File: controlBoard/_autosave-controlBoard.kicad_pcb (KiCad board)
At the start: 2 copper layers, 37.5 x 35 mm, 33 parts, among them J2 Servo, SW1 SW_Push, SW2 SW_Push, U1 ATmega328P-AU, U2 PCA9685BS, U3 AP2112K-3.3TRG1, Y1 Crystal

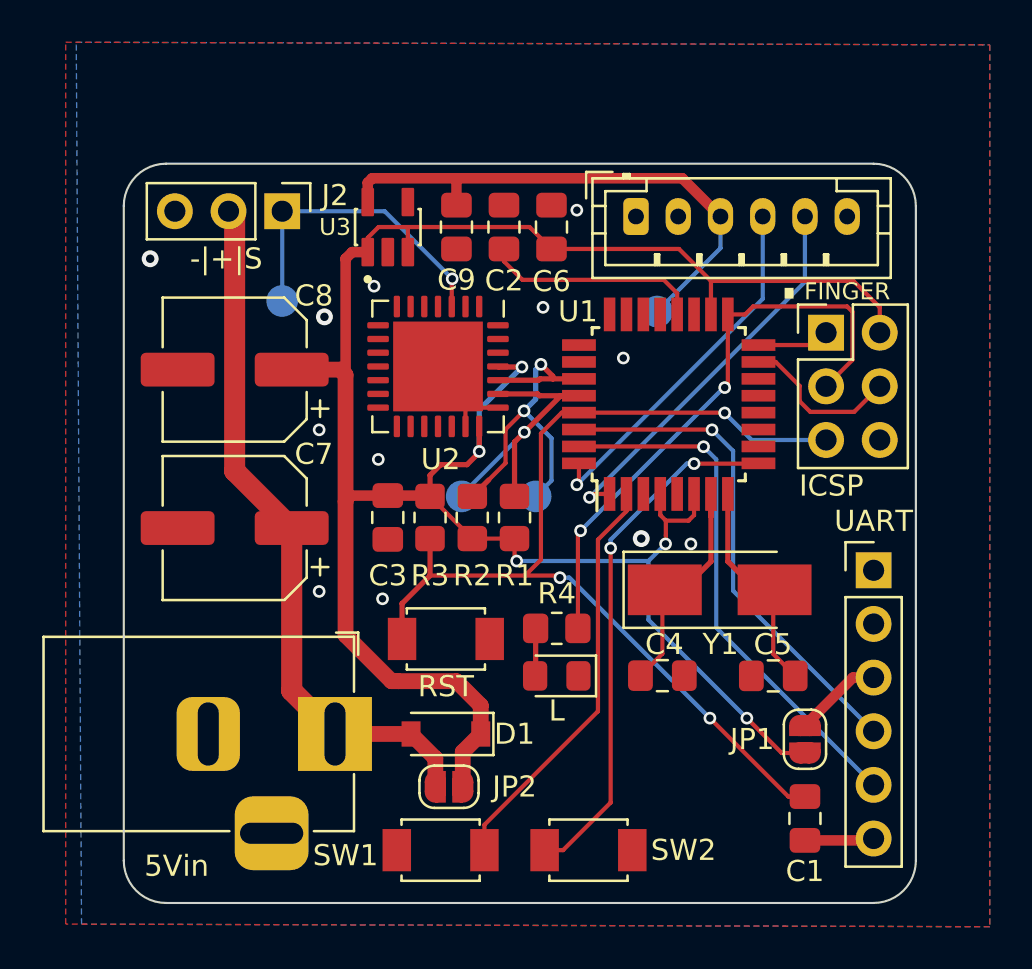
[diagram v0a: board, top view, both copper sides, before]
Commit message: Added decoupling cap for fingerprint reader, generated gerbers
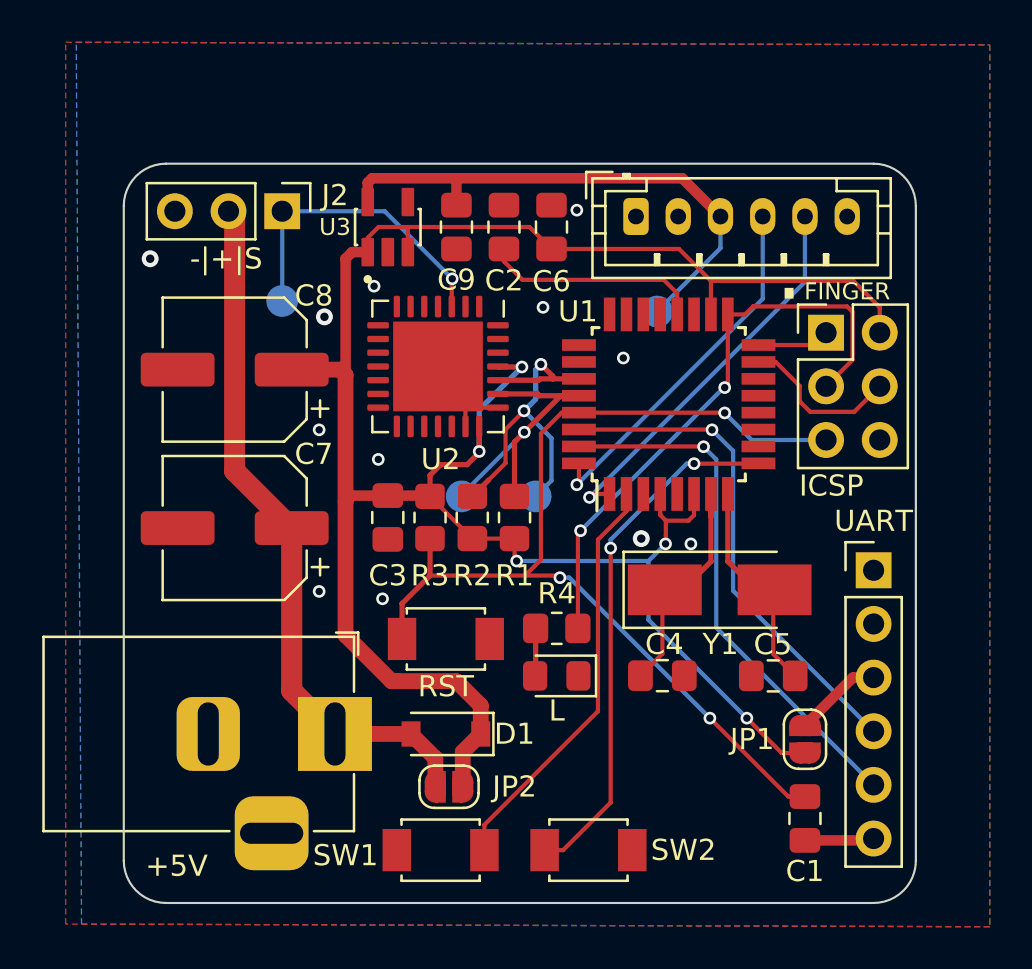
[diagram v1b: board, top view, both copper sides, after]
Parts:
- renumbered 5Vin to +5V
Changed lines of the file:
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@@
   (general
     (thickness 1.6)
-    (drawings 33)
+    (drawings 32)
     (tracks 236)
     (zones 0)
@@
       (layerselection 0x010fc_ffffffff)
       (usegerberextensions true)
-      (usegerberattributes true)
+      (usegerberattributes false)
       (usegerberadvancedattributes false)
       (creategerberjobfile false)
@@
       (effects (font (size 0.5 0.5) (thickness 0.08)))
     )
-    (pad 1 smd roundrect (at -1.0375 0 270) (size 1.175 1.45) (layers F.Cu F.Paste F.Mask) (roundrect_rratio 0.212766)
+    (pad 1 smd roundrect (at -1.0375 0 270) (size 1.175 1.45) (layers F.Cu F.Paste F.Mask) (roundrect_rratio 0.2127659574468085)
       (net 53 +3V3))
-    (pad 2 smd roundrect (at 1.0375 0 270) (size 1.175 1.45) (layers F.Cu F.Paste F.Mask) (roundrect_rratio 0.212766)
+    (pad 2 smd roundrect (at 1.0375 0 270) (size 1.175 1.45) (layers F.Cu F.Paste F.Mask) (roundrect_rratio 0.2127659574468085)
       (net 2 GND))
     (model ${KISYS3DMOD}/Capacitor_SMD.3dshapes/C_0805_2012Metric.wrl
@@
       (effects (font (size 0.5 0.5) (thickness 0.08)))
     )
-    (pad 2 smd roundrect (at 1 0) (size 1.2 1.4) (layers F.Cu F.Paste F.Mask) (roundrect_rratio 0.208333)
+    (pad 2 smd roundrect (at 1 0) (size 1.2 1.4) (layers F.Cu F.Paste F.Mask) (roundrect_rratio 0.2083325)
       (net 12 /SCK))
-    (pad 1 smd roundrect (at -1 0) (size 1.2 1.4) (layers F.Cu F.Paste F.Mask) (roundrect_rratio 0.208333)
+    (pad 1 smd roundrect (at -1 0) (size 1.2 1.4) (layers F.Cu F.Paste F.Mask) (roundrect_rratio 0.2083325)
       (net 52 "Net-(D2-Pad2)"))
     (model ${KISYS3DMOD}/Resistor_SMD.3dshapes/R_0805_2012Metric.wrl
@@
       (effects (font (size 0.5 0.5) (thickness 0.08)))
     )
-    (pad 2 smd roundrect (at 1.025 0 180) (size 1.15 1.4) (layers F.Cu F.Paste F.Mask) (roundrect_rratio 0.217391)
+    (pad 2 smd roundrect (at 1.025 0 180) (size 1.15 1.4) (layers F.Cu F.Paste F.Mask) (roundrect_rratio 0.2173904347826087)
       (net 52 "Net-(D2-Pad2)"))
-    (pad 1 smd roundrect (at -1.025 0 180) (size 1.15 1.4) (layers F.Cu F.Paste F.Mask) (roundrect_rratio 0.217391)
+    (pad 1 smd roundrect (at -1.025 0 180) (size 1.15 1.4) (layers F.Cu F.Paste F.Mask) (roundrect_rratio 0.2173904347826087)
       (net 2 GND))
     (model ${KISYS3DMOD}/LED_SMD.3dshapes/LED_0805_2012Metric.wrl
@@
       (effects (font (size 0.5 0.5) (thickness 0.08)))
     )
-    (pad 2 smd roundrect (at 1 0 90) (size 1.2 1.4) (layers F.Cu F.Paste F.Mask) (roundrect_rratio 0.208333)
+    (pad 2 smd roundrect (at 1 0 90) (size 1.2 1.4) (layers F.Cu F.Paste F.Mask) (roundrect_rratio 0.2083325)
       (net 15 /SDA))
-    (pad 1 smd roundrect (at -1 0 90) (size 1.2 1.4) (layers F.Cu F.Paste F.Mask) (roundrect_rratio 0.208333)
+    (pad 1 smd roundrect (at -1 0 90) (size 1.2 1.4) (layers F.Cu F.Paste F.Mask) (roundrect_rratio 0.2083325)
       (net 1 +5V))
     (model ${KISYS3DMOD}/Resistor_SMD.3dshapes/R_0805_2012Metric.wrl
@@
       (effects (font (size 0.5 0.5) (thickness 0.08)))
     )
-    (pad 2 smd roundrect (at 1 0 90) (size 1.2 1.4) (layers F.Cu F.Paste F.Mask) (roundrect_rratio 0.208333)
+    (pad 2 smd roundrect (at 1 0 90) (size 1.2 1.4) (layers F.Cu F.Paste F.Mask) (roundrect_rratio 0.2083325)
       (net 14 /SCL))
-    (pad 1 smd roundrect (at -1 0 90) (size 1.2 1.4) (layers F.Cu F.Paste F.Mask) (roundrect_rratio 0.208333)
+    (pad 1 smd roundrect (at -1 0 90) (size 1.2 1.4) (layers F.Cu F.Paste F.Mask) (roundrect_rratio 0.2083325)
       (net 1 +5V))
     (model ${KISYS3DMOD}/Resistor_SMD.3dshapes/R_0805_2012Metric.wrl
@@
     (descr "DC Barrel Jack")
     (tags "Power Jack")
-    (fp_text reference 5Vin (at -7.5 6.25) (layer F.SilkS)
+    (fp_text reference +5V (at -7.5 6.25) (layer F.SilkS)
       (effects (font (size 1 1) (thickness 0.15)))
     )
@@
     (pad 29 smd rect (at 0 0 270) (size 4.25 4.25) (layers F.Cu F.Mask)
       (net 2 GND))
-    (pad "" smd roundrect (at -1.42 -1.42 270) (size 1.14 1.14) (layers F.Paste) (roundrect_rratio 0.2192973684210526))
-    (pad "" smd roundrect (at -1.42 0 270) (size 1.14 1.14) (layers F.Paste) (roundrect_rratio 0.2192973684210526))
-    (pad "" smd roundrect (at -1.42 1.42 270) (size 1.14 1.14) (layers F.Paste) (roundrect_rratio 0.2192973684210526))
-    (pad "" smd roundrect (at 0 -1.42 270) (size 1.14 1.14) (layers F.Paste) (roundrect_rratio 0.2192973684210526))
-    (pad "" smd roundrect (at 0 0 270) (size 1.14 1.14) (layers F.Paste) (roundrect_rratio 0.2192973684210526))
-    (pad "" smd roundrect (at 0 1.42 270) (size 1.14 1.14) (layers F.Paste) (roundrect_rratio 0.2192973684210526))
-    (pad "" smd roundrect (at 1.42 -1.42 270) (size 1.14 1.14) (layers F.Paste) (roundrect_rratio 0.2192973684210526))
-    (pad "" smd roundrect (at 1.42 0 270) (size 1.14 1.14) (layers F.Paste) (roundrect_rratio 0.2192973684210526))
-    (pad "" smd roundrect (at 1.42 1.42 270) (size 1.14 1.14) (layers F.Paste) (roundrect_rratio 0.2192973684210526))
+    (pad "" smd roundrect (at -1.42 -1.42 270) (size 1.14 1.14) (layers F.Paste) (roundrect_rratio 0.2192964912280702))
+    (pad "" smd roundrect (at -1.42 0 270) (size 1.14 1.14) (layers F.Paste) (roundrect_rratio 0.2192964912280702))
+    (pad "" smd roundrect (at -1.42 1.42 270) (size 1.14 1.14) (layers F.Paste) (roundrect_rratio 0.2192964912280702))
+    (pad "" smd roundrect (at 0 -1.42 270) (size 1.14 1.14) (layers F.Paste) (roundrect_rratio 0.2192964912280702))
+    (pad "" smd roundrect (at 0 0 270) (size 1.14 1.14) (layers F.Paste) (roundrect_rratio 0.2192964912280702))
+    (pad "" smd roundrect (at 0 1.42 270) (size 1.14 1.14) (layers F.Paste) (roundrect_rratio 0.2192964912280702))
+    (pad "" smd roundrect (at 1.42 -1.42 270) (size 1.14 1.14) (layers F.Paste) (roundrect_rratio 0.2192964912280702))
+    (pad "" smd roundrect (at 1.42 0 270) (size 1.14 1.14) (layers F.Paste) (roundrect_rratio 0.2192964912280702))
+    (pad "" smd roundrect (at 1.42 1.42 270) (size 1.14 1.14) (layers F.Paste) (roundrect_rratio 0.2192964912280702))
     (model ${KISYS3DMOD}/Package_DFN_QFN.3dshapes/QFN-28-1EP_6x6mm_P0.65mm_EP4.25x4.25mm.wrl
       (at (xyz 0 0 0))
@@
     (arrow2b (pts (xy 140.75 107.5) (xy 141.876504 106.913579)))
   )
-  (target plus (at 140.75 101) (size 5) (width 0.05) (layer Edge.Cuts))
   (gr_text "  +5V|MISO\nMOSI|SCK\n   - |RST " (at 169 76.5) (layer B.SilkS)
     (effects (font (size 1 1) (thickness 0.15)) (justify mirror))
